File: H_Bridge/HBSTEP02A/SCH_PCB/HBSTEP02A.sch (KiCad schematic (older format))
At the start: 8 parts, among them J1 Umin ... Umax, M1 HOLE, M2 HOLE, M3 HOLE, M4 HOLE

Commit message: uklid
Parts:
- added C?: 4u7, symbol C
- added C? (x3): 100nF, symbol C
- added C?: C, symbol C
- added D? (x2): D_Schottky_Small, symbol D_Schottky_Small
- added J? (x2): ENCN/DCO, symbol HEADER_2x01_PARALLEL
- added J? (x5): HEADER_2x01_PARALLEL, symbol HEADER_2x01_PARALLEL
- added J?: CSN/CFG3, symbol HEADER_2x01_PARALLEL
- added J?: SCK/CFG2, symbol HEADER_2x01_PARALLEL
- added J?: SID/NAI/CFG1, symbol HEADER_2x01_PARALLEL
- added J?: SDO/NAO/CFG0, symbol HEADER_2x01_PARALLEL
- added J? (x2): CONN1_1, symbol CONN1_1
- added J?: CPO, symbol HEADER_2x01_PARALLEL
- added J?: CLK, symbol HEADER_2x01_PARALLEL
- added L? (x2): 100nH, symbol L_Small
- added R?: 1k, symbol R_Small
- added R?: R_Small, symbol R_Small
- added U?: TMC5130A, symbol TMC5130A
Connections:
- net labels added: 5VOUT, GNDA, GNDPWR
- net labels removed: GND
- wire segments 17 -> 59
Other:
- moved on the sheet: C1, C2, D1, J1

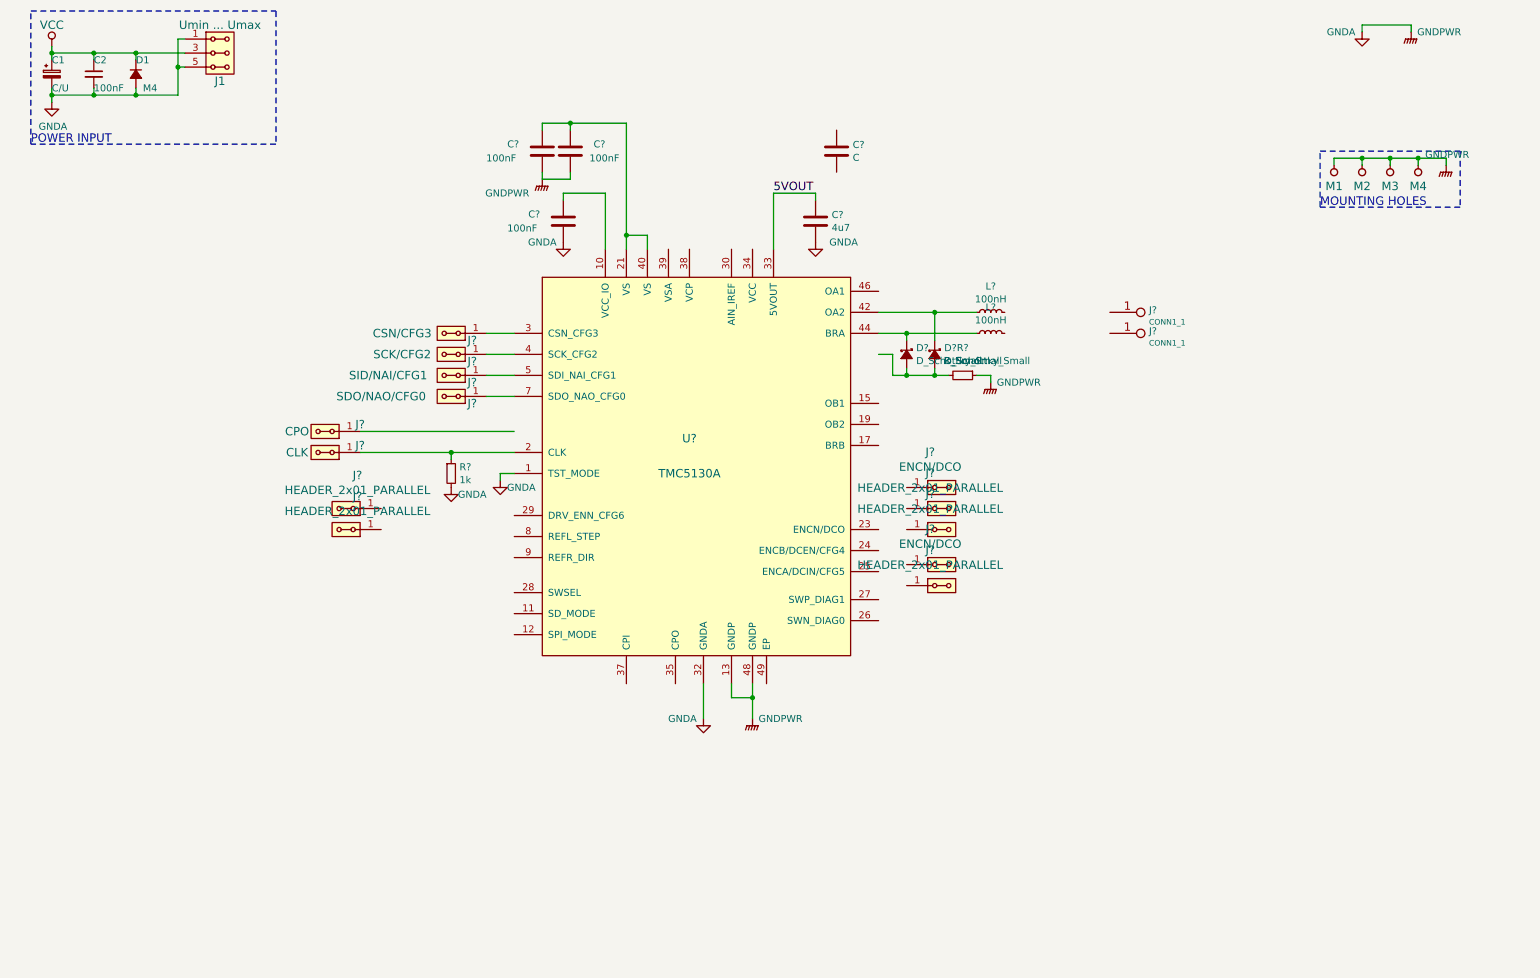
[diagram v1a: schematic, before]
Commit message: nakresleno schema. Vygenerovan netlist a zalozen PCB.
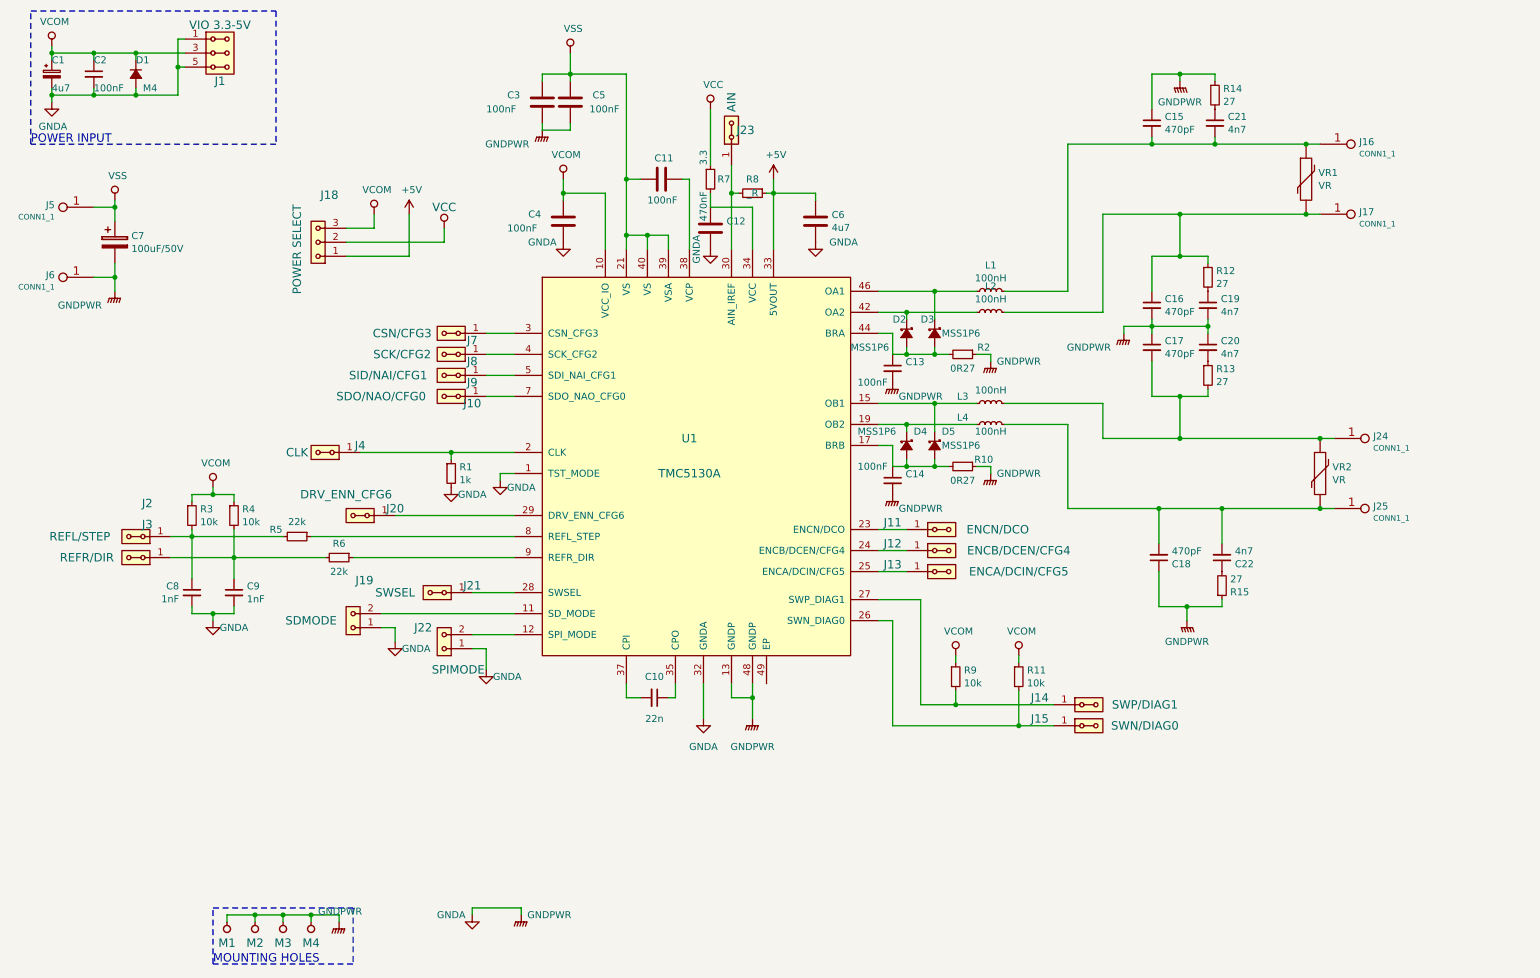
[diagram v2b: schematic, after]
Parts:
- removed C?: C, symbol C
- removed J?: CPO, symbol HEADER_2x01_PARALLEL
- removed J? (x2): HEADER_2x01_PARALLEL, symbol HEADER_2x01_PARALLEL
- added C10: 22n, Capacitors_SMD:C_0805, symbol C_Small
- added C11: 100nF, Capacitors_SMD:C_0805, symbol C
- added C12: 470nF, Capacitors_SMD:C_0805, symbol C
- added C13, C14: 100nF, Capacitors_SMD:C_0805, symbol C_Small
- added C15, C16, C17, C18: 470pF, Capacitors_SMD:C_0805, symbol C_Small
- added C19, C20, C21, C22: 4n7, Capacitors_SMD:C_0805, symbol C_Small
- added C7: 100uF/50V, Capacitors_ThroughHole:C_Radial_D10_L13_P5, symbol CP
- added C8, C9: 1nF, Capacitors_SMD:C_0805, symbol C_Small
- added D4, D5: MSS1P6, HBSTEP02A:SCHOT_D_MSS1P6, symbol D_Schottky_Small
- added J18: POWER SELECT, Mlab_Pin_Headers:Straight_1x03, symbol HEADER_1x03
- added J19: SDMODE, Mlab_Pin_Headers:Straight_1x02, symbol HEADER_1x02
- added J2: REFL/STEP, Mlab_Pin_Headers:Straight_1x02, symbol HEADER_2x01_PARALLEL
- added J20: DRV_ENN_CFG6, Mlab_Pin_Headers:Straight_1x02, symbol HEADER_2x01_PARALLEL
- added J21: SWSEL, Mlab_Pin_Headers:Straight_1x02, symbol HEADER_2x01_PARALLEL
- added J22: SPIMODE, Mlab_Pin_Headers:Straight_1x02, symbol HEADER_1x02
- added J23: AIN, Mlab_Pin_Headers:Straight_1x02, symbol HEADER_2x01_PARALLEL
- added J24, J25, J5, J6: CONN1_1, Mlab_Con:WAGO256, symbol CONN1_1
- added J3: REFR/DIR, Mlab_Pin_Headers:Straight_1x02, symbol HEADER_2x01_PARALLEL
- added L3, L4: 100nH, HBSTEP02A:Inductor_4.5_4.1, symbol L_Small
- added R10: 0R27, Resistors_SMD:R_1206_HandSoldering, symbol R_Small
- added R11, R3, R4, R9: 10k, Resistors_SMD:R_0805, symbol R_Small
- added R12, R13, R14, R15: 27, Resistors_SMD:R_0805, symbol R_Small
- added R5, R6: 22k, Resistors_SMD:R_0805, symbol R_Small
- added R7: 3.3, Resistors_SMD:R_0805, symbol R_Small
- added R8: _R, Resistors_SMD:R_0805_HandSoldering, symbol R_Small
- added VR1, VR2: VR, Capacitors_SMD:C_0805, symbol VR
- C1: value C/U -> 4u7; footprint (none) -> Capacitors_SMD:C_0805
- C2: footprint (none) -> Capacitors_SMD:C_0805
- C3, C4, C5, C6: renamed from C?; footprint (none) -> Capacitors_SMD:C_0805
- D1: footprint (none) -> Diodes_SMD:SMA_Handsoldering
- D2, D3: renamed from D?; value D_Schottky_Small -> MSS1P6; footprint (none) -> HBSTEP02A:SCHOT_D_MSS1P6
- J1: value Umin ... Umax -> VIO 3.3-5V; footprint (none) -> Mlab_Pin_Headers:Straight_2x03
- J10, J11, J4, J7, J8, J9: renamed from J?; footprint (none) -> Mlab_Pin_Headers:Straight_1x02
- J12: renamed from J?; value HEADER_2x01_PARALLEL -> ENCB/DCEN/CFG4; footprint (none) -> Mlab_Pin_Headers:Straight_1x02
- J13: renamed from J?; value HEADER_2x01_PARALLEL -> ENCA/DCIN/CFG5; footprint (none) -> Mlab_Pin_Headers:Straight_1x02
- J14: renamed from J?; value ENCN/DCO -> SWP/DIAG1; footprint (none) -> Mlab_Pin_Headers:Straight_1x02
- J15: renamed from J?; value HEADER_2x01_PARALLEL -> SWN/DIAG0; footprint (none) -> Mlab_Pin_Headers:Straight_1x02
- J16, J17: renamed from J?; footprint (none) -> Mlab_Con:WAGO256
- L1, L2: renamed from L?; footprint (none) -> HBSTEP02A:Inductor_4.5_4.1
- M1, M2, M3, M4: footprint (none) -> Mlab_Mechanical:MountingHole_3mm
- R1: renamed from R?; footprint (none) -> Resistors_SMD:R_0805
- R2: renamed from R?; value R_Small -> 0R27; footprint (none) -> Resistors_SMD:R_1206_HandSoldering
- U1: renamed from U?; footprint (none) -> Housings_QFP:TQFP-48-1EP_7x7mm_Pitch0.5mm
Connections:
- net labels added: +5V, VCOM, VSS
- net labels removed: 5VOUT
- wire segments 59 -> 164
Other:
- moved on the sheet: C3, C5, D2, D3, J11, J12, J13, J14, J15, J16, J17, L1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

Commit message: prvni cast pcb
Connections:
- net GNDA: now also C21.1, C22.1; no longer R14.1, R15.1
- net at C15.2, J16.1 (P1), L1.2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: now also R14.2; no longer C21.2
- net at C18.2, J25.1 (P1), L4.2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: now also R15.2; no longer C22.2
- new net: C21.2, R14.1
- new net: C22.2, R15.1
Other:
- moved on the sheet: C21, C22, R14, R15
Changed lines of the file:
@@
 LIBS:graphic
 LIBS:hc11
-LIBS:header
 LIBS:intel
 LIBS:interface
@@
 LIBS:logo
 LIBS:maxim
-LIBS:mechanical
 LIBS:memory
 LIBS:microchip_dspic33dsc
@@
 LIBS:xilinx
 LIBS:Zilog
-LIBS:MLAB_CONNECTORS
-LIBS:MLAB_Jumpers
 LIBS:HBSTEP02A-cache
 EELAYER 25 0
@@
 L C_Small C21
 U 1 1 56E39A9D
+P 9200 1350
+F 0 "C21" H 9292 1396 50  0000 L CNN
+F 1 "4n7" H 9292 1304 50  0000 L CNN
+F 2 "Capacitors_SMD:C_0805" H 9200 1350 50  0001 C CNN
+F 3 "" H 9200 1350 50  0000 C CNN
+	1    9200 1350
+	1    0    0    -1
+$EndComp
+$Comp
+L R_Small R14
+U 1 1 56E39AA3
 P 9200 1550
-F 0 "C21" H 9292 1596 50  0000 L CNN
-F 1 "4n7" H 9292 1504 50  0000 L CNN
-F 2 "Capacitors_SMD:C_0805" H 9200 1550 50  0001 C CNN
+F 0 "R14" H 9259 1596 50  0000 L CNN
+F 1 "27" H 9259 1504 50  0000 L CNN
+F 2 "Resistors_SMD:R_0805" H 9200 1550 50  0001 C CNN
 F 3 "" H 9200 1550 50  0000 C CNN
 	1    9200 1550
-	1    0    0    -1
-$EndComp
-$Comp
-L R_Small R14
-U 1 1 56E39AA3
-P 9200 1350
-F 0 "R14" H 9259 1396 50  0000 L CNN
-F 1 "27" H 9259 1304 50  0000 L CNN
-F 2 "Resistors_SMD:R_0805" H 9200 1350 50  0001 C CNN
-F 3 "" H 9200 1350 50  0000 C CNN
-	1    9200 1350
 	1    0    0    -1
 $EndComp
@@
 L C_Small C22
 U 1 1 56E3E914
+P 9250 4850
+F 0 "C22" H 9342 4896 50  0000 L CNN
+F 1 "4n7" H 9342 4804 50  0000 L CNN
+F 2 "Capacitors_SMD:C_0805" H 9250 4850 50  0001 C CNN
+F 3 "" H 9250 4850 50  0000 C CNN
+	1    9250 4850
+	1    0    0    1
+$EndComp
+$Comp
+L R_Small R15
+U 1 1 56E3E91A
 P 9250 4650
-F 0 "C22" H 9342 4696 50  0000 L CNN
-F 1 "4n7" H 9342 4604 50  0000 L CNN
-F 2 "Capacitors_SMD:C_0805" H 9250 4650 50  0001 C CNN
+F 0 "R15" H 9309 4696 50  0000 L CNN
+F 1 "27" H 9309 4604 50  0000 L CNN
+F 2 "Resistors_SMD:R_0805" H 9250 4650 50  0001 C CNN
 F 3 "" H 9250 4650 50  0000 C CNN
 	1    9250 4650
 	1    0    0    1
 $EndComp
-$Comp
-L R_Small R15
-U 1 1 56E3E91A
-P 9250 4850
-F 0 "R15" H 9309 4896 50  0000 L CNN
-F 1 "27" H 9309 4804 50  0000 L CNN
-F 2 "Resistors_SMD:R_0805" H 9250 4850 50  0001 C CNN
-F 3 "" H 9250 4850 50  0000 C CNN
-	1    9250 4850
-	1    0    0    1
-$EndComp
